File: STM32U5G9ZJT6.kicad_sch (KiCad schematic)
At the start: 4 parts, among them U1 STM32U5G9ZJTxQ, Y1 16MHz

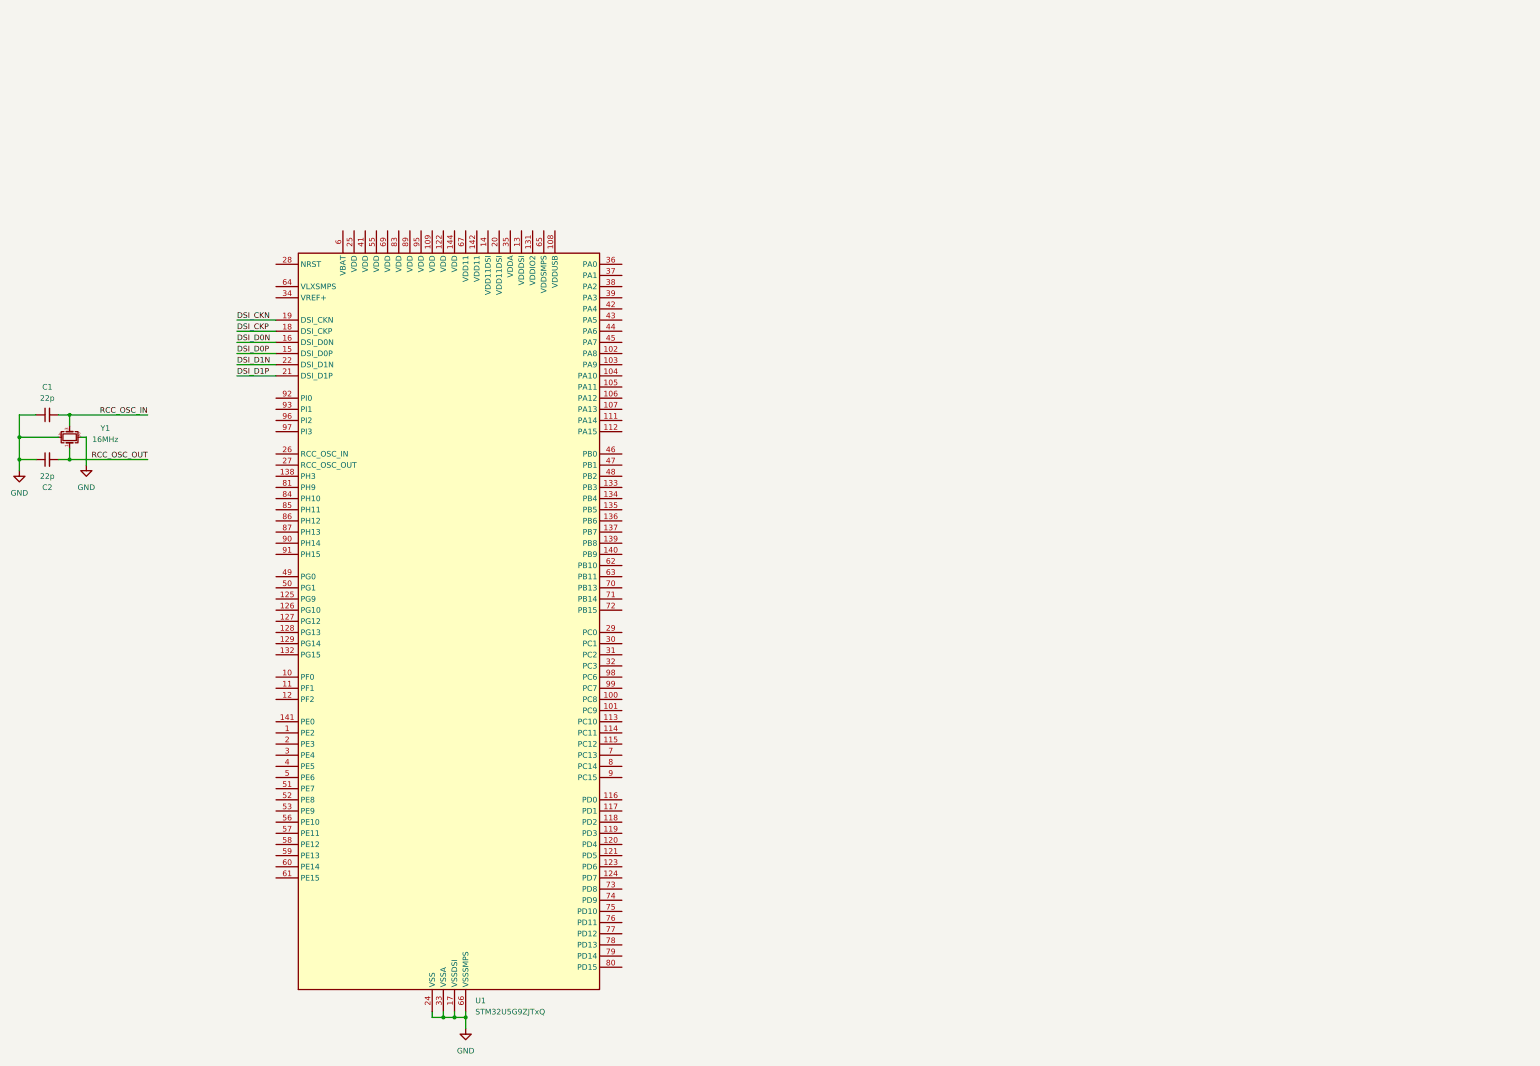
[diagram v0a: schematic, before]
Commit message: Add Octospi Flash, LCD 40P, 50P, MIPI
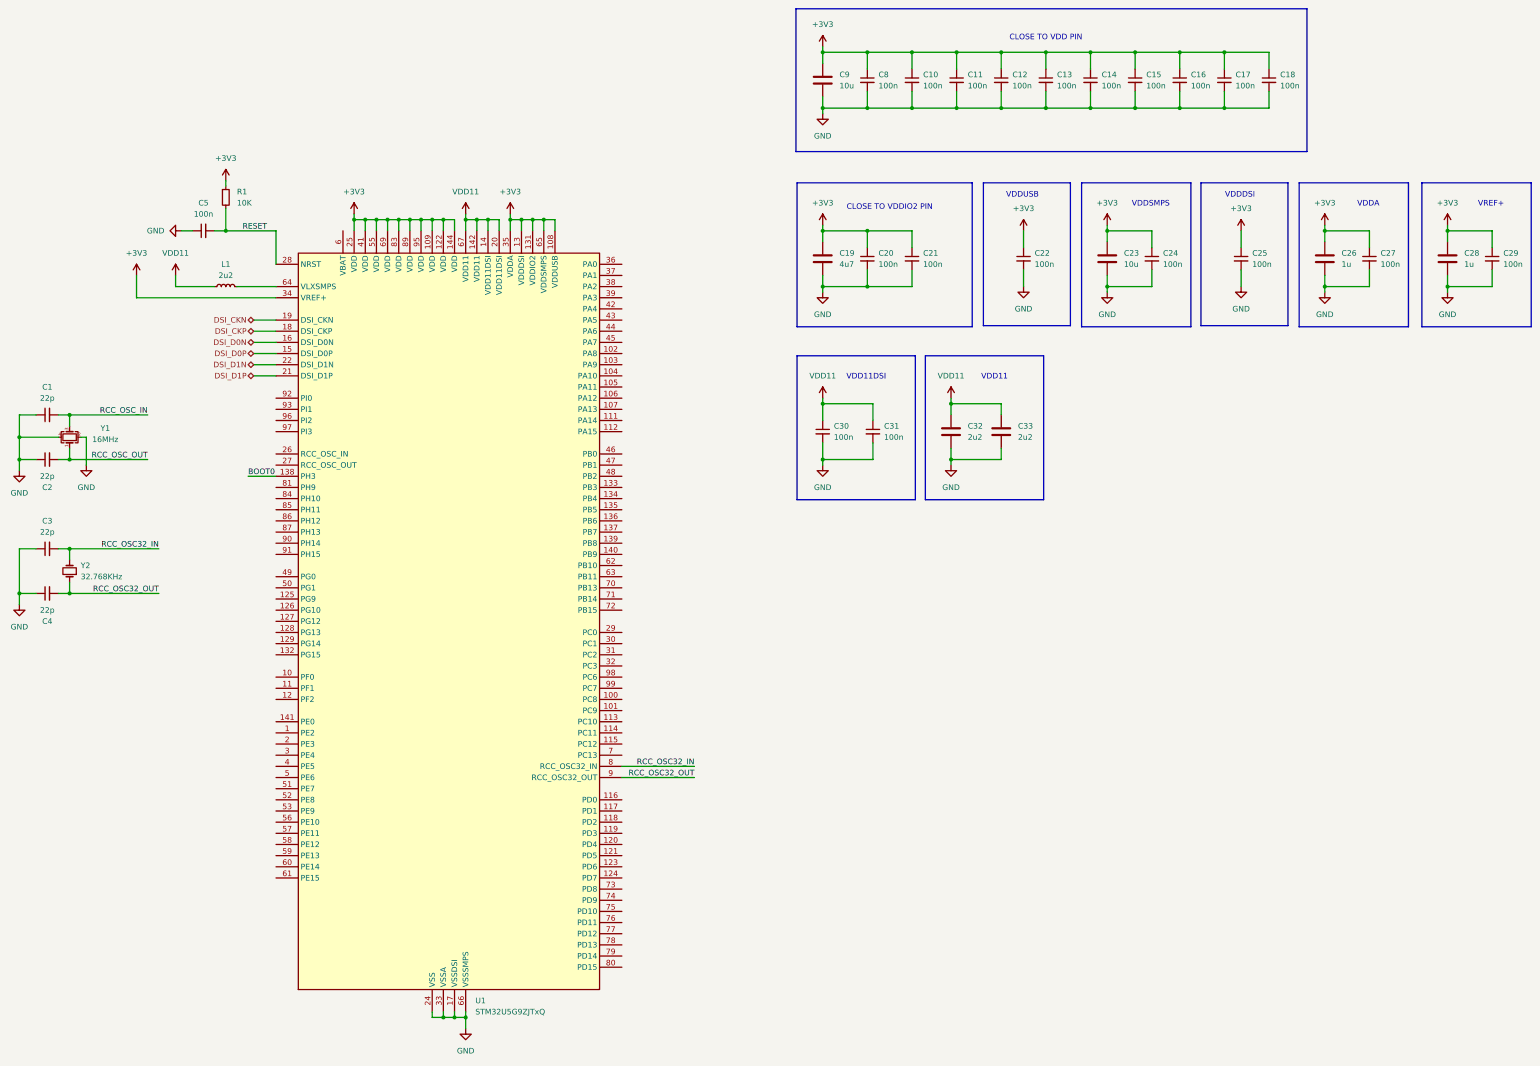
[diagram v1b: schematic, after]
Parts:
- added C10, C11, C12, C13, C14, C15, C16, C17, C18, C20, C21, C22, C24, C25, C27, C29, C30, C31, C5, C8: 100n, Capacitor_SMD:C_0402_1005Metric, symbol Device:C_Small
- added C19: 4u7, Capacitor_SMD:C_0603_1608Metric, symbol Device:C
- added C23, C9: 10u, Capacitor_SMD:C_0603_1608Metric, symbol Device:C
- added C26, C28: 1u, Capacitor_SMD:C_0603_1608Metric, symbol Device:C
- added C3, C4: 22p, Capacitor_SMD:C_0402_1005Metric, symbol Device:C_Small
- added C32, C33: 2u2, Capacitor_SMD:C_0603_1608Metric, symbol Device:C
- added L1: 2u2, Inductor_SMD:L_0805_2012Metric, symbol Device:L_Small
- added R1: 10K, Resistor_SMD:R_0402_1005Metric, symbol Device:R_Small
- added Y2: 32.768KHz, Crystal:Crystal_SMD_2012-2Pin_2.0x1.2mm, symbol Device:Crystal_Small
- C1, C2: footprint (none) -> Capacitor_SMD:C_0402_1005Metric
- Y1: footprint (none) -> Crystal:Crystal_SMD_2520-4Pin_2.5x2.0mm
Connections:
- net GND: now also C10.2, C11.2, C12.2, C13.2, C14.2, C15.2, C16.2, C17.2, C18.2, C19.2, C20.2, C21.2, C22.2, C23.2, C24.2, C25.2, C26.2, C27.2, C28.2, C29.2, C3.1, C30.2, C31.2, C32.2, C33.2, C4.1, C5.1, C8.2, C9.2
- net +3V3: now reaches U1.108 (VDDUSB)
- net +3V3: now also U1.109 (VDD), U1.122 (VDD), U1.13 (VDDDSI), U1.131 (VDDIO2), U1.144 (VDD), U1.25 (VDD), U1.34 (VREF+), U1.35 (VDDA), U1.41 (VDD), U1.55 (VDD), U1.65 (VDDSMPS), U1.69 (VDD), U1.83 (VDD), U1.89 (VDD), U1.95 (VDD), C10.1, C11.1, C12.1, C13.1, C14.1, C15.1, C16.1, C17.1, C18.1, C19.1, C20.1, C21.1, C22.1, C23.1, C24.1, C25.1, C26.1, C27.1, C28.1, C29.1, C8.1, C9.1, R1.1
- net BOOT0: now reaches U1.138 (PH3)
- net VDD11: now reaches U1.14 (VDD11DSI)
- net VDD11: now also U1.142 (VDD11), U1.20 (VDD11DSI), U1.67 (VDD11), C30.1, C31.1, C32.1, C33.1, L1.1
- net RESET: now reaches U1.28 (NRST)
- net RESET: now also C5.2, R1.2
- net at U1.64 (VLXSMPS): now also L1.2
- net RCC_OSC32_IN: now reaches U1.8 (PC14)
- net RCC_OSC32_IN: now also C3.2, Y2.2
- net RCC_OSC32_OUT: now reaches U1.9 (PC15)
- net RCC_OSC32_OUT: now also C4.2, Y2.1
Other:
- note added: "CLOSE TO VDD PIN"
- note added: "CLOSE TO VDDIO2 PIN"
- note added: "VDD11"
- note added: "VDD11DSI"
- note added: "VDDA"
- note added: "VDDDSI"
- note added: "VDDSMPS"
- note added: "VDDUSB"
- note added: "VREF+"
